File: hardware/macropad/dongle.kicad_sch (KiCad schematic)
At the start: 17 parts, among them J1 USB_A, J2 Conn_01x04_Pin, J6 Conn_02x03_Counter_Clockwise, SW10 SW_Push, U1 NRF24L01_Breakout, U2 AP2112K-3.3, U3 STM32F103C8Tx

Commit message: schematic halfass done
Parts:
- removed C1, C2: C, symbol Device:C
- removed C3, C4, C5, C7, C8, C9: 100n, symbol Device:C
- removed C6: 10u, symbol Device:C
- removed J2: Conn_01x04_Pin, Connector_PinHeader_2.54mm:PinHeader_1x04_P2.54mm_Horizontal, symbol Connector:Conn_01x04_Pin
- removed J6: Conn_02x03_Counter_Clockwise, symbol Connector_Generic:Conn_02x03_Counter_Clockwise
- removed R1: 1.5K, symbol Device:R
- removed SW10: SW_Push, symbol Switch:SW_Push
- removed U1: NRF24L01_Breakout, RF_Module:nRF24L01_Breakout, symbol RF:NRF24L01_Breakout
- removed U2: AP2112K-3.3, Package_TO_SOT_SMD:SOT-23-5, symbol Regulator_Linear:AP2112K-3.3
- removed U3: STM32F103C8Tx, Package_QFP:LQFP-48_7x7mm_P0.5mm, symbol MCU_ST_STM32F1:STM32F103C8Tx
- added C10, C21: 10u, Capacitor_SMD:C_0805_2012Metric, symbol Device:C
- added C11, C15: 12p, Capacitor_SMD:C_0805_2012Metric, symbol Device:C
- added C12, C14, C16, C17, C19, C20: 100n, Capacitor_SMD:C_0805_2012Metric, symbol Device:C
- added C13, C18: 1u, Capacitor_SMD:C_0805_2012Metric, symbol Device:C
- added J7: Conn_01x04_Pin, Connector_PinHeader_2.54mm:PinHeader_1x04_P2.54mm_Horizontal, symbol Connector:Conn_01x04_Pin
- added J9: Conn_02x03_Counter_Clockwise, Connector_PinHeader_2.54mm:PinHeader_2x03_P2.54mm_Vertical, symbol Connector_Generic:Conn_02x03_Counter_Clockwise
- added R11: 1.5K, Resistor_SMD:R_0805_2012Metric, symbol Device:R
- added R12: 10k, Resistor_SMD:R_0805_2012Metric, symbol Device:R
- added SW12: SW_Push, Button_Switch_SMD:SW_DIP_SPSTx01_Slide_6.7x4.1mm_W6.73mm_P2.54mm_LowProfile_JPin, symbol Switch:SW_Push
- added U4: AP2112K-3.3, Package_TO_SOT_SMD:SOT-23-5, symbol Regulator_Linear:AP2112K-3.3
- added U5: STM32F103C8Tx, Package_QFP:LQFP-48_7x7mm_P0.5mm, symbol MCU_ST_STM32F1:STM32F103C8Tx
- added U6: NRF24L01_Breakout, RF_Module:nRF24L01_Breakout, symbol RF:NRF24L01_Breakout
- added Y1: 8Mhz, Crystal:Crystal_SMD_3225-4Pin_3.2x2.5mm, symbol Device:Crystal_GND24
- J8: renamed from J1; footprint (none) -> Connector_USB:USB_A_Connfly_DS1095
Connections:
- net +3.3V: now also C10.1, C12.1, C14.1, C16.1, C17.1, C18.1, C19.1, C21.1, J7.1 (Pin_1), J9.3 (Pin_3), J9.4 (Pin_4), R11.1, U4.5 (VOUT), U5.1 (VBAT), U5.24 (VDD), U5.36 (VDD), U5.48 (VDD), U5.9 (VDDA), U6.2 (VCC)
- net BOOT0: now also R12.1, U5.44 (BOOT0)
- net BOOT1: now also J9.2 (Pin_2), U5.20 (PB2)
- net GND: now also C10.2, C11.2, C12.2, C13.2, C14.2, C15.2, C16.2, C17.2, C18.2, C19.2, C20.1, C21.2, J7.4 (Pin_4), J9.1 (Pin_1), J9.6 (Pin_6), SW12.2, U4.2 (GND), U5.23 (VSS), U5.35 (VSS), U5.47 (VSS), U5.8 (VSSA), U6.1 (GND), Y1.2, Y1.4
- net NRST: now also C20.2, SW12.1, U5.7 (NRST)
- net PA5: now also U5.15 (PA5), U6.5 (SCK)
- net PA6: now also U5.16 (PA6), U6.7 (MISO)
- net PA7: now also U5.17 (PA7), U6.6 (MOSI)
- net PB0: now also U5.18 (PB0), U6.4 (~{CSN})
- net PB1: now also U5.19 (PB1), U6.3 (CE)
- net PB10: now also U5.21 (PB10), U6.8 (IRQ)
- net SWCLK: now also J7.3 (Pin_3), U5.37 (PA14)
- net SWDIO: now also J7.2 (Pin_2), U5.34 (PA13)
- net USB_D+: now also R11.2, U5.33 (PA12)
- net USB_D-: now also U5.32 (PA11)
- net VDD: now also C13.1, U4.1 (VIN)
- new net: J9.5 (Pin_5), R12.2
- new net HSE_IN: C11.1, U5.5 (PD0), Y1.1
- new net HSE_OUT: C15.1, U5.6 (PD1), Y1.3

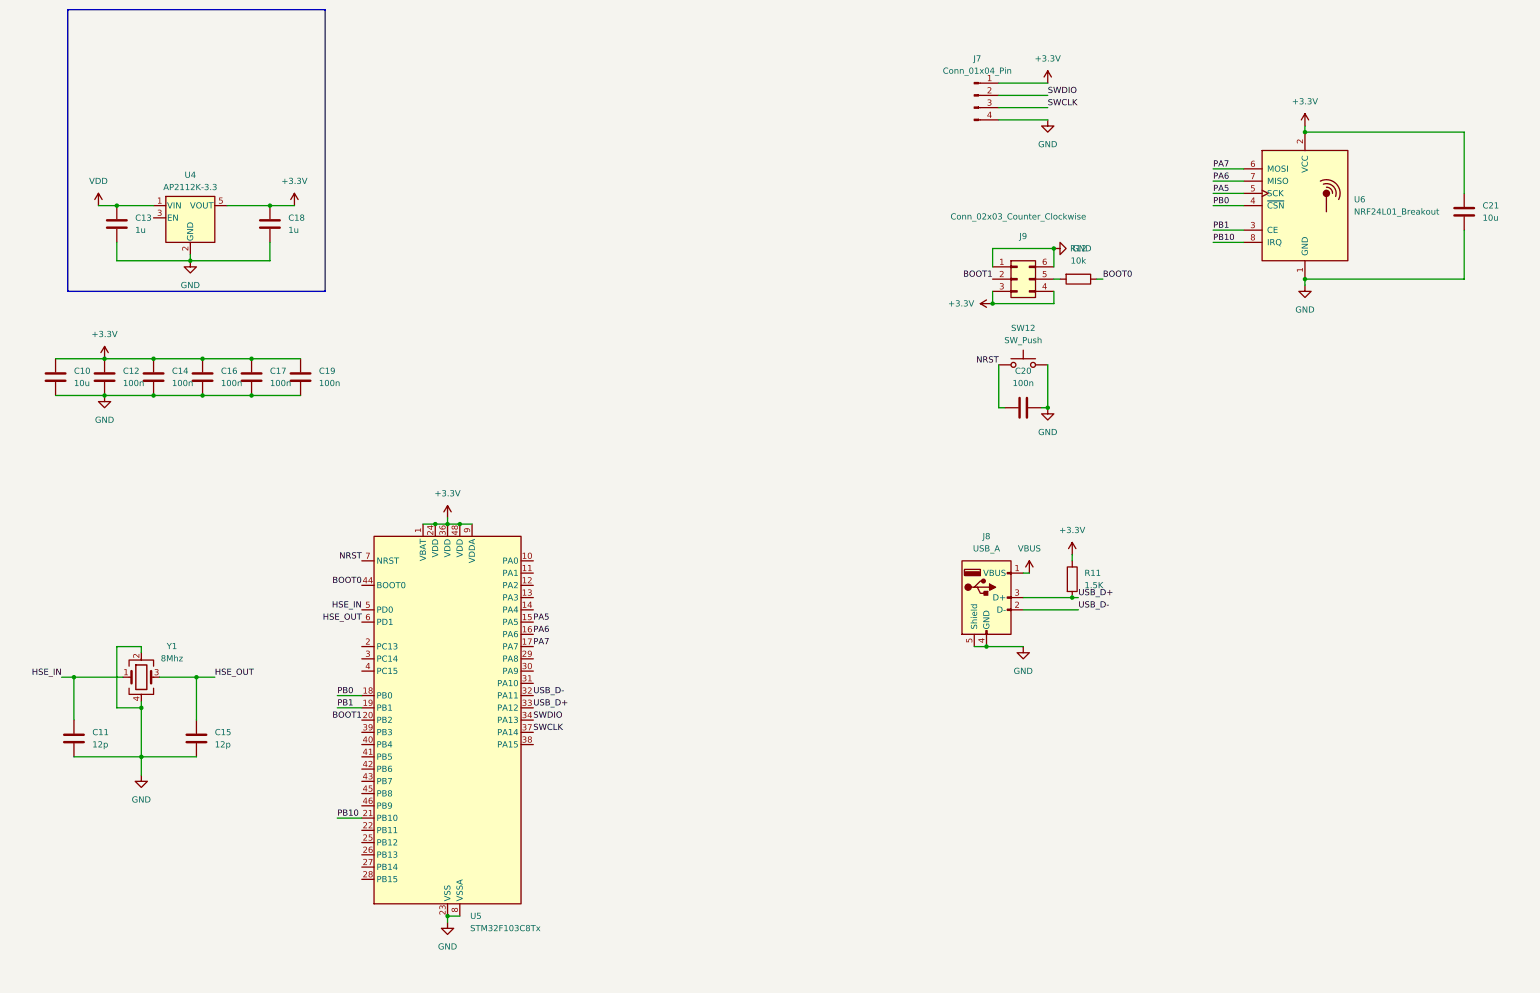
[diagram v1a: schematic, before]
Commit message: ERC satisfied. Net names changed for not global
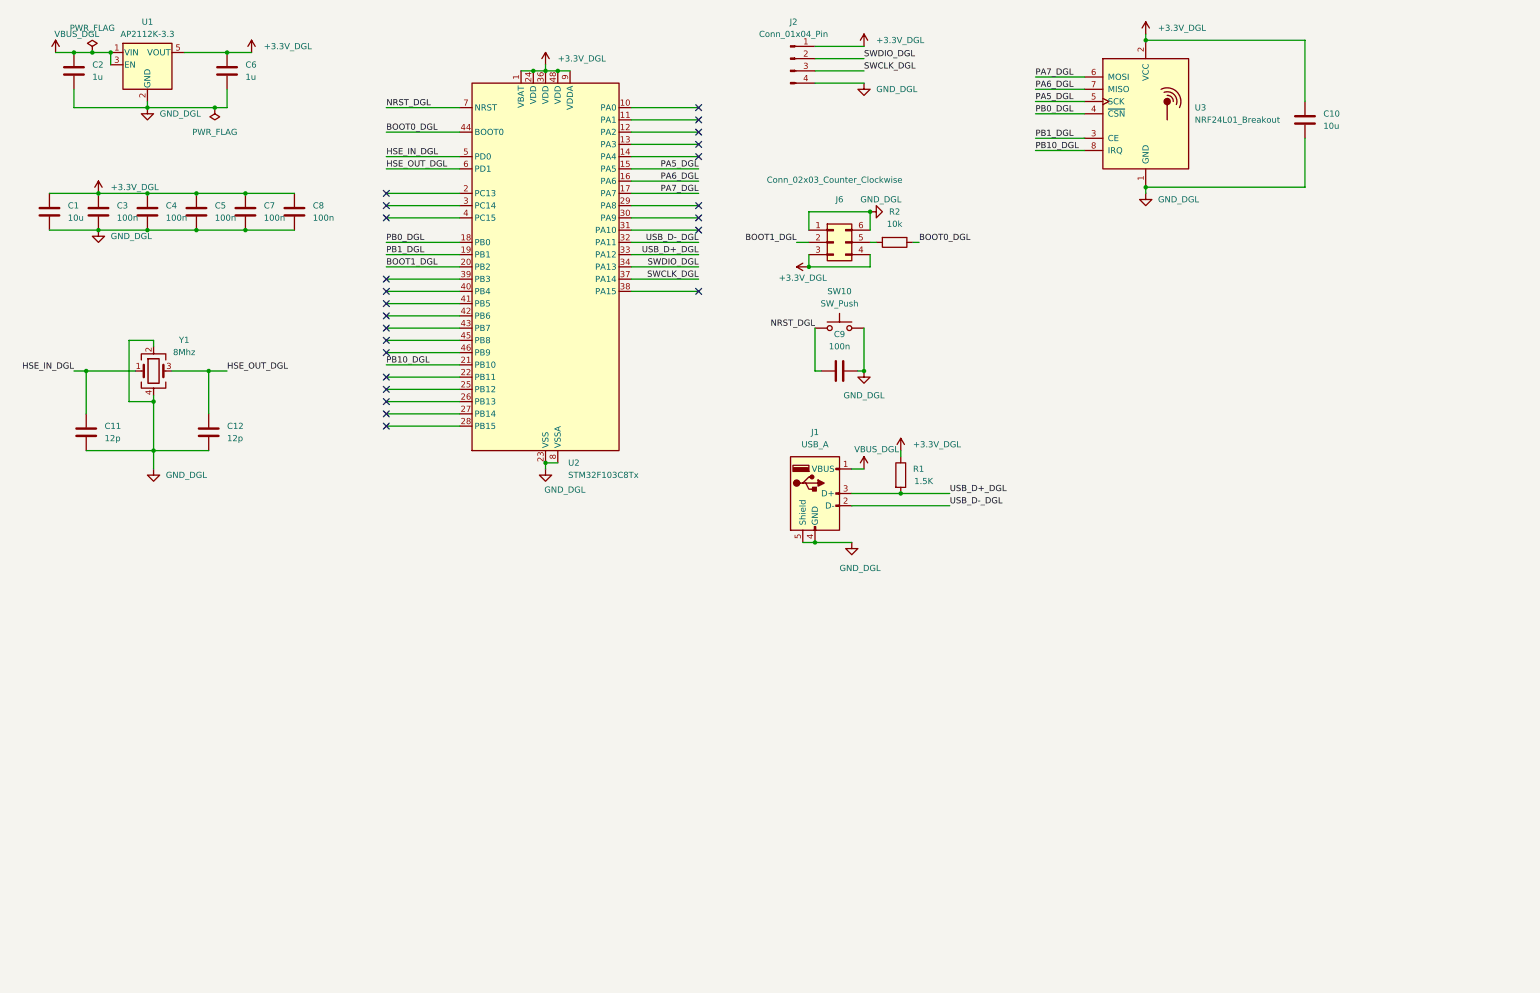
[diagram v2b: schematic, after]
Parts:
- renumbered C10 to C1, C21 to C10, C15 to C12, C13 to C2, C12 to C3, C14 to C4, C16 to C5, C18 to C6, C17 to C7, C19 to C8, C20 to C9, J8 to J1, J7 to J2, J9 to J6, R11 to R1, R12 to R2, SW12 to SW10, U4 to U1, U5 to U2, U6 to U3
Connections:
- net VBUS is gone; now on net VBUS_DGL: J1.1 (VBUS)
- net VDD is gone; now on net VBUS_DGL: C2.1, U1.1 (VIN)
- net VBUS_DGL: now reaches U1.3 (EN)
- net +3.3V renamed +3.3V_DGL
- net BOOT0 renamed BOOT0_DGL
- net BOOT1 renamed BOOT1_DGL
- net GND renamed GND_DGL
- net HSE_IN renamed HSE_IN_DGL
- net HSE_OUT renamed HSE_OUT_DGL
- net NRST renamed NRST_DGL
- net PA5 renamed PA5_DGL
- net PA6 renamed PA6_DGL
- net PA7 renamed PA7_DGL
- net PB0 renamed PB0_DGL
- net PB1 renamed PB1_DGL
- net PB10 renamed PB10_DGL
- net SWCLK renamed SWCLK_DGL
- net SWDIO renamed SWDIO_DGL
- net USB_D+ renamed USB_D+_DGL
- net USB_D- renamed USB_D-_DGL
- no-connect marks 0 -> 24
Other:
- moved on the sheet: C1, C10, C11, C12, C2, C3, C4, C5, C6, C7, C8, C9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

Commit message: changed load capacitance, added oscillator for pad
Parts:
- C11, C12: value 12p -> 25p
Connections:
- net BOOT0_DGL is gone; now on net GND_DGL: R2.1, U2.44 (BOOT0)
- net BOOT1_DGL is gone; now on net GND_DGL: J6.2 (Pin_2), U2.20 (PB2)
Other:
- moved on the sheet: J6, R2

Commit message: update oscillator + passives'
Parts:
- removed J6: Conn_02x03_Counter_Clockwise, Connector_PinHeader_2.54mm:PinHeader_2x03_P2.54mm_Vertical, symbol Connector_Generic:Conn_02x03_Counter_Clockwise
- removed R2: 10k, Resistor_SMD:R_0805_2012Metric, symbol Device:R
- C11, C12: value 25p -> 18p

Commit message: updated footprints
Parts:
- C11: footprint Capacitor_SMD:C_0805_2012Metric -> Capacitor_SMD:C_0603_1608Metric
- C12: renamed from C3; footprint Capacitor_SMD:C_0805_2012Metric -> Capacitor_SMD:C_0603_1608Metric
- C13: renamed from C4; footprint Capacitor_SMD:C_0805_2012Metric -> Capacitor_SMD:C_0603_1608Metric
- C14: renamed from C5; footprint Capacitor_SMD:C_0805_2012Metric -> Capacitor_SMD:C_0603_1608Metric
- C15: renamed from C12; footprint Capacitor_SMD:C_0805_2012Metric -> Capacitor_SMD:C_0603_1608Metric
- C19: renamed from C7; footprint Capacitor_SMD:C_0805_2012Metric -> Capacitor_SMD:C_0603_1608Metric
- C20: renamed from C8; footprint Capacitor_SMD:C_0805_2012Metric -> Capacitor_SMD:C_0603_1608Metric
- C21: renamed from C9; footprint Capacitor_SMD:C_0805_2012Metric -> Capacitor_SMD:C_0603_1608Metric
- J5: renamed from J1; footprint Connector_USB:USB_A_Connfly_DS1095 -> (none)
- R3: renamed from R1; footprint Resistor_SMD:R_0805_2012Metric -> Resistor_SMD:R_0603_1608Metric
- U1: footprint Package_TO_SOT_SMD:SOT-23-5 -> (none)
- renumbered C2 to C10, C6 to C16, C10 to C22, C1 to C7, J2 to J3, SW10 to SW14, U2 to U4, U3 to U5, Y1 to Y2

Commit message: updated footprints
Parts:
- SW14: footprint Button_Switch_SMD:SW_DIP_SPSTx01_Slide_6.7x4.1mm_W6.73mm_P2.54mm_LowProfile_JPin -> Button_Switch_SMD:SW_Push_1P1T_NO_E-Switch_TL3301NxxxxxG
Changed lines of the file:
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@@
 			)
 		)
-		(property "Footprint" "Button_Switch_SMD:SW_DIP_SPSTx01_Slide_6.7x4.1mm_W6.73mm_P2.54mm_LowProfile_JPin"
+		(property "Footprint" "Button_Switch_SMD:SW_Push_1P1T_NO_E-Switch_TL3301NxxxxxG"
 			(at 186.69 76.2 0)
 			(effects
